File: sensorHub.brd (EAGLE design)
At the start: 70 x 70 mm, 11 parts

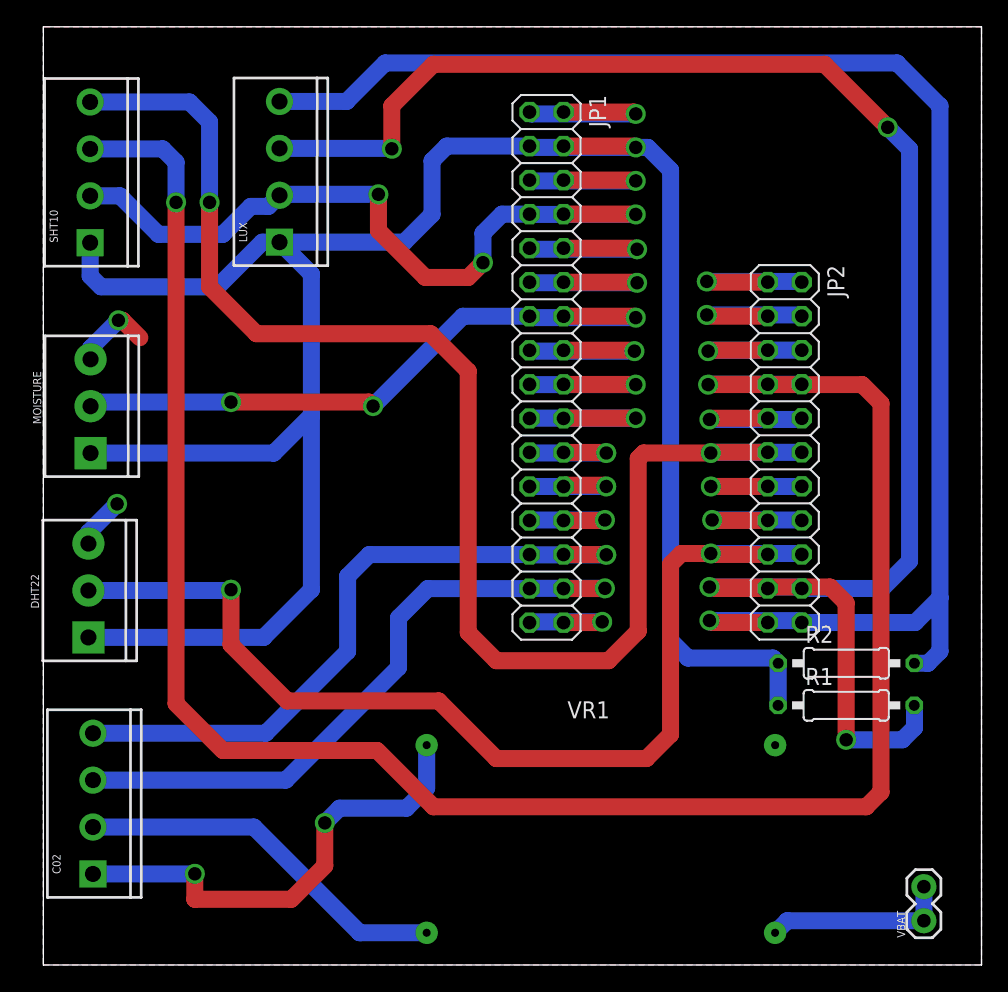
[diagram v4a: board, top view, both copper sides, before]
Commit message: Replaces the 22 double header with the 24 double header
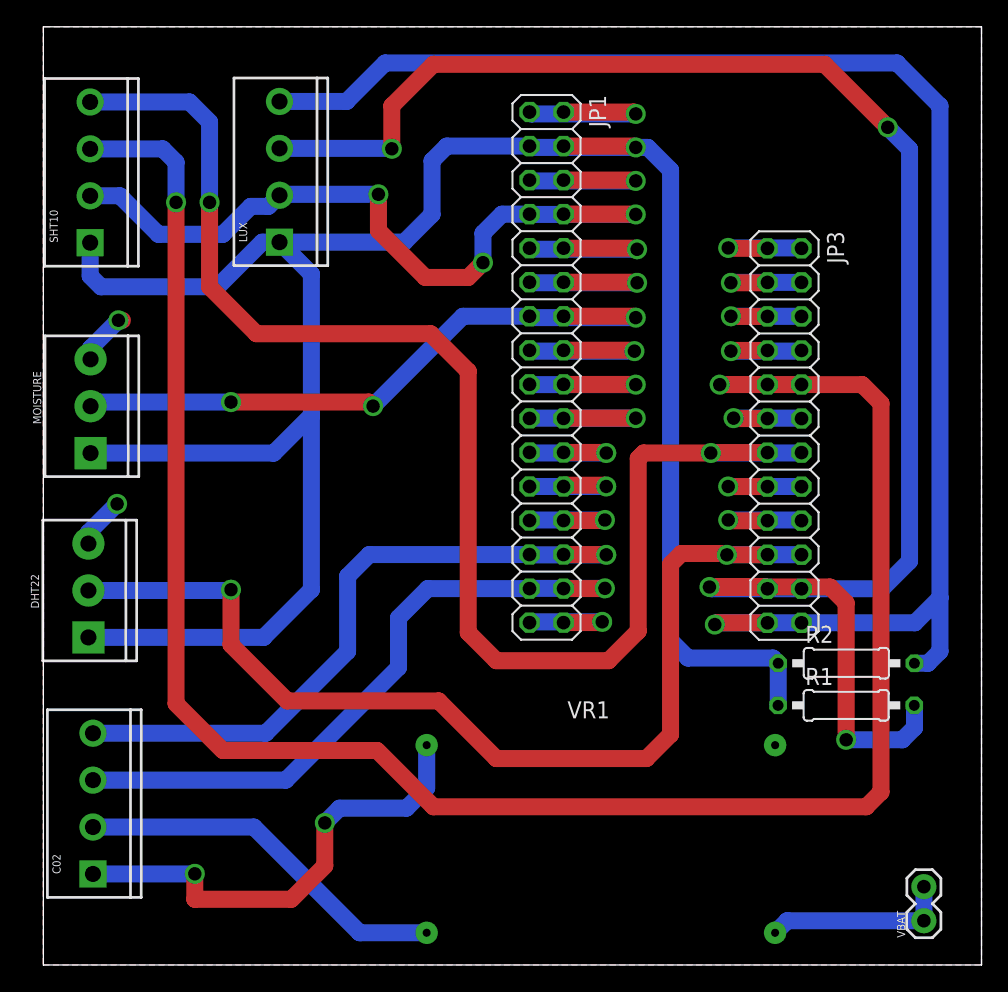
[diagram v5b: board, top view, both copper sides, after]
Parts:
- removed JP2: (no value), pinhead:2X11
- added JP3: (no value), pinhead:2X12
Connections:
- removed net N$19: JP2.5, JP2.6
- removed net N$21: JP2.10, JP2.9
- removed net N$23: JP2.13, JP2.14
- removed net N$24: JP2.15, JP2.16
- new net N$14: JP3.7, JP3.8
- new net N$15: JP3.11, JP3.12
- new net N$2: JP3.1, JP3.2
- new net N$4: JP3.3, JP3.4
- new net N$7: JP3.5, JP3.6
- net 10_SDA: now also JP3.13, JP3.14; no longer JP2.11, JP2.12
- net 12_SCL: now also JP3.10, JP3.9; no longer JP2.7, JP2.8
- net D5: now also JP3.19, JP3.20; no longer JP2.17, JP2.18
- net N$17: now also JP3.15, JP3.16; no longer JP2.1, JP2.2
- net N$18: now also JP3.17, JP3.18; no longer JP2.3, JP2.4
- net SCL: now also JP3.21, JP3.22; no longer JP2.19, JP2.20
- net SDA: now also JP3.23, JP3.24; no longer JP2.21, JP2.22
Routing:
- net N$19: track 11.5 -> 0.00 mm, vias 1 -> 0
- net N$21: track 11.3 -> 0.00 mm, vias 1 -> 0
- net N$23: track 11.0 -> 0.00 mm, vias 1 -> 0
- net N$24: track 10.9 -> 0.00 mm, vias 1 -> 0
- net N$2: track 0.00 -> 8.42 mm, vias 0 -> 1
- net N$14: track 0.00 -> 8.04 mm, vias 0 -> 1
- net N$4: track 0.00 -> 8.02 mm, vias 0 -> 1
- net N$7: track 0.00 -> 8.01 mm, vias 0 -> 1
- net N$15: track 0.00 -> 7.62 mm, vias 0 -> 1
- net N$18: track 11.7 -> 8.44 mm
- net N$17: track 11.7 -> 8.41 mm
- net 12_SCL: track 157.4 -> 154.8 mm
- net GND: track 101.0 -> 99.2 mm
- net D5: track 79.0 -> 77.7 mm
- net SDA: track 117.2 -> 116.4 mm
